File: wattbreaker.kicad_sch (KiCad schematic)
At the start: 33 parts, among them J1 Stomp, J2 Power, U1 TL072

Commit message: v0.1: initial revision
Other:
- moved on the sheet: J1, J2
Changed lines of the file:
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@@
   (junction (at 156.845 55.245) (diameter 0.9144) (color 0 0 0 0))
   (junction (at 160.02 55.245) (diameter 0.9144) (color 0 0 0 0))
-  (no_connect (at 51.435 109.855))
+  (no_connect (at 145.415 87.63))
   (wire (pts (xy 25.4 69.215) (xy 29.845 69.215))
     (stroke (width 0) (type solid) (color 0 0 0 0))
@@
     (stroke (width 0) (type solid) (color 0 0 0 0))
   )
-  (wire (pts (xy 34.29 107.315) (xy 51.435 107.315))
-    (stroke (width 0) (type solid) (color 0 0 0 0))
-  )
-  (wire (pts (xy 34.29 108.585) (xy 34.29 107.315))
-    (stroke (width 0) (type solid) (color 0 0 0 0))
-  )
   (wire (pts (xy 38.1 88.265) (xy 38.1 91.44))
     (stroke (width 0) (type solid) (color 0 0 0 0))
@@
     (stroke (width 0) (type solid) (color 0 0 0 0))
   )
-  (wire (pts (xy 43.815 104.775) (xy 51.435 104.775))
-    (stroke (width 0) (type solid) (color 0 0 0 0))
-  )
-  (wire (pts (xy 43.815 112.395) (xy 51.435 112.395))
-    (stroke (width 0) (type solid) (color 0 0 0 0))
-  )
   (wire (pts (xy 52.07 27.305) (xy 52.07 35.56))
     (stroke (width 0) (type solid) (color 0 0 0 0))
@@
     (stroke (width 0) (type solid) (color 0 0 0 0))
   )
-  (wire (pts (xy 72.39 107.315) (xy 72.39 105.41))
-    (stroke (width 0) (type solid) (color 0 0 0 0))
-  )
-  (wire (pts (xy 72.39 109.855) (xy 74.295 109.855))
-    (stroke (width 0) (type solid) (color 0 0 0 0))
-  )
-  (wire (pts (xy 72.39 111.76) (xy 72.39 109.855))
-    (stroke (width 0) (type solid) (color 0 0 0 0))
-  )
-  (wire (pts (xy 74.295 107.315) (xy 72.39 107.315))
-    (stroke (width 0) (type solid) (color 0 0 0 0))
-  )
   (wire (pts (xy 74.93 27.305) (xy 78.105 27.305))
     (stroke (width 0) (type solid) (color 0 0 0 0))
@@
     (stroke (width 0) (type solid) (color 0 0 0 0))
   )
+  (wire (pts (xy 128.27 85.09) (xy 145.415 85.09))
+    (stroke (width 0) (type solid) (color 0 0 0 0))
+  )
+  (wire (pts (xy 128.27 86.36) (xy 128.27 85.09))
+    (stroke (width 0) (type solid) (color 0 0 0 0))
+  )
   (wire (pts (xy 135.89 55.245) (xy 137.795 55.245))
     (stroke (width 0) (type solid) (color 0 0 0 0))
   )
+  (wire (pts (xy 137.795 82.55) (xy 145.415 82.55))
+    (stroke (width 0) (type solid) (color 0 0 0 0))
+  )
+  (wire (pts (xy 137.795 90.17) (xy 145.415 90.17))
+    (stroke (width 0) (type solid) (color 0 0 0 0))
+  )
   (wire (pts (xy 145.415 55.245) (xy 147.32 55.245))
     (stroke (width 0) (type solid) (color 0 0 0 0))
@@
   )
   (wire (pts (xy 160.02 67.945) (xy 160.02 69.85))
+    (stroke (width 0) (type solid) (color 0 0 0 0))
+  )
+  (wire (pts (xy 166.37 85.09) (xy 166.37 83.185))
+    (stroke (width 0) (type solid) (color 0 0 0 0))
+  )
+  (wire (pts (xy 166.37 87.63) (xy 168.275 87.63))
+    (stroke (width 0) (type solid) (color 0 0 0 0))
+  )
+  (wire (pts (xy 166.37 89.535) (xy 166.37 87.63))
+    (stroke (width 0) (type solid) (color 0 0 0 0))
+  )
+  (wire (pts (xy 168.275 85.09) (xy 166.37 85.09))
     (stroke (width 0) (type solid) (color 0 0 0 0))
   )
@@
     (effects (font (size 1.27 1.27)) (justify right))
   )
-  (global_label "IN" (shape input) (at 43.815 104.775 180)    (property "Intersheet References" "${INTERSHEET_REFS}" (id 0) (at 37.9427 104.6956 0)
+  (global_label "IN" (shape input) (at 137.795 82.55 180)    (property "Intersheet References" "${INTERSHEET_REFS}" (id 0) (at 131.9227 82.4706 0)
       (effects (font (size 1.27 1.27)) (justify right) hide)
     )
     (effects (font (size 1.27 1.27)) (justify right))
   )
-  (global_label "OUT" (shape output) (at 43.815 112.395 180)    (property "Intersheet References" "${INTERSHEET_REFS}" (id 0) (at 36.2493 112.3156 0)
+  (global_label "OUT" (shape output) (at 137.795 90.17 180)    (property "Intersheet References" "${INTERSHEET_REFS}" (id 0) (at 130.2293 90.0906 0)
       (effects (font (size 1.27 1.27)) (justify right) hide)
     )
@@
     )
   )
-  (symbol (lib_id "power:+9V") (at 72.39 105.41 0) (unit 1)
-    (in_bom yes) (on_board yes)
-    (property "Reference" "#PWR07" (id 0) (at 72.39 109.22 0)
-      (effects (font (size 1.27 1.27)) hide)
-    )
-    (property "Value" "+9V" (id 1) (at 72.7583 101.0856 0))
-    (property "Footprint" "" (id 2) (at 72.39 105.41 0)
-      (effects (font (size 1.27 1.27)) hide)
-    )
-    (property "Datasheet" "" (id 3) (at 72.39 105.41 0)
-      (effects (font (size 1.27 1.27)) hide)
-    )
-  )
   (symbol (lib_id "power:+9V") (at 86.36 70.485 0) (unit 1)
     (in_bom yes) (on_board yes)
@@
     )
   )
+  (symbol (lib_id "power:+9V") (at 166.37 83.185 0) (unit 1)
+    (in_bom yes) (on_board yes)
+    (property "Reference" "#PWR07" (id 0) (at 166.37 86.995 0)
+      (effects (font (size 1.27 1.27)) hide)
+    )
+    (property "Value" "+9V" (id 1) (at 166.7383 78.8606 0))
+    (property "Footprint" "" (id 2) (at 166.37 83.185 0)
+      (effects (font (size 1.27 1.27)) hide)
+    )
+    (property "Datasheet" "" (id 3) (at 166.37 83.185 0)
+      (effects (font (size 1.27 1.27)) hide)
+    )
+  )
   (symbol (lib_id "power:GND") (at 29.845 82.55 0) (unit 1)
     (in_bom yes) (on_board yes)
@@
     )
   )
-  (symbol (lib_id "power:GND") (at 34.29 108.585 0) (unit 1)
-    (in_bom yes) (on_board yes)
-    (property "Reference" "#PWR02" (id 0) (at 34.29 114.935 0)
-      (effects (font (size 1.27 1.27)) hide)
-    )
-    (property "Value" "GND" (id 1) (at 34.4043 112.9094 0))
-    (property "Footprint" "" (id 2) (at 34.29 108.585 0)
-      (effects (font (size 1.27 1.27)) hide)
-    )
-    (property "Datasheet" "" (id 3) (at 34.29 108.585 0)
-      (effects (font (size 1.27 1.27)) hide)
-    )
-  )
   (symbol (lib_id "power:GND") (at 59.69 75.565 0) (unit 1)
     (in_bom yes) (on_board yes)
@@
     )
   )
-  (symbol (lib_id "power:GND") (at 72.39 111.76 0) (unit 1)
-    (in_bom yes) (on_board yes)
-    (property "Reference" "#PWR08" (id 0) (at 72.39 118.11 0)
-      (effects (font (size 1.27 1.27)) hide)
-    )
-    (property "Value" "GND" (id 1) (at 72.5043 116.0844 0))
-    (property "Footprint" "" (id 2) (at 72.39 111.76 0)
-      (effects (font (size 1.27 1.27)) hide)
-    )
-    (property "Datasheet" "" (id 3) (at 72.39 111.76 0)
-      (effects (font (size 1.27 1.27)) hide)
-    )
-  )
   (symbol (lib_id "power:GND") (at 99.06 95.885 0) (unit 1)
     (in_bom yes) (on_board yes)
@@
     )
   )
+  (symbol (lib_id "power:GND") (at 128.27 86.36 0) (unit 1)
+    (in_bom yes) (on_board yes)
+    (property "Reference" "#PWR02" (id 0) (at 128.27 92.71 0)
+      (effects (font (size 1.27 1.27)) hide)
+    )
+    (property "Value" "GND" (id 1) (at 128.3843 90.6844 0))
+    (property "Footprint" "" (id 2) (at 128.27 86.36 0)
+      (effects (font (size 1.27 1.27)) hide)
+    )
+    (property "Datasheet" "" (id 3) (at 128.27 86.36 0)
+      (effects (font (size 1.27 1.27)) hide)
+    )
+  )
   (symbol (lib_id "power:GND") (at 160.02 69.85 0) (unit 1)
     (in_bom yes) (on_board yes)
@@
     )
     (property "Datasheet" "" (id 3) (at 160.02 69.85 0)
+      (effects (font (size 1.27 1.27)) hide)
+    )
+  )
+  (symbol (lib_id "power:GND") (at 166.37 89.535 0) (unit 1)
+    (in_bom yes) (on_board yes)
+    (property "Reference" "#PWR08" (id 0) (at 166.37 95.885 0)
+      (effects (font (size 1.27 1.27)) hide)
+    )
+    (property "Value" "GND" (id 1) (at 166.4843 93.8594 0))
+    (property "Footprint" "" (id 2) (at 166.37 89.535 0)
+      (effects (font (size 1.27 1.27)) hide)
+    )
+    (property "Datasheet" "" (id 3) (at 166.37 89.535 0)
       (effects (font (size 1.27 1.27)) hide)
     )
@@
     )
   )
-  (symbol (lib_id "Connector:Conn_01x02_Female") (at 79.375 107.315 0) (unit 1)
-    (in_bom yes) (on_board yes)
-    (property "Reference" "J2" (id 0) (at 80.0863 107.8928 0)
-      (effects (font (size 1.27 1.27)) (justify left))
-    )
-    (property "Value" "Power" (id 1) (at 80.086 110.192 0)
-      (effects (font (size 1.27 1.27)) (justify left))
-    )
-    (property "Footprint" "rockola_kicad_footprints:Power_Header_2pin" (id 2) (at 79.375 107.315 0)
-      (effects (font (size 1.27 1.27)) hide)
-    )
-    (property "Datasheet" "~" (id 3) (at 79.375 107.315 0)
+  (symbol (lib_id "Connector:Conn_01x02_Female") (at 173.355 85.09 0) (unit 1)
+    (in_bom yes) (on_board yes)
+    (property "Reference" "J2" (id 0) (at 174.0663 85.6678 0)
+      (effects (font (size 1.27 1.27)) (justify left))
+    )
+    (property "Value" "Power" (id 1) (at 174.066 87.967 0)
+      (effects (font (size 1.27 1.27)) (justify left))
+    )
+    (property "Footprint" "rockola_kicad_footprints:Power_Header_2pin" (id 2) (at 173.355 85.09 0)
+      (effects (font (size 1.27 1.27)) hide)
+    )
+    (property "Datasheet" "~" (id 3) (at 173.355 85.09 0)
       (effects (font (size 1.27 1.27)) hide)
     )
@@
     )
   )
-  (symbol (lib_id "Connector:Conn_01x04_Female") (at 56.515 107.315 0) (unit 1)
-    (in_bom yes) (on_board yes)
-    (property "Reference" "J1" (id 0) (at 57.2263 107.8928 0)
-      (effects (font (size 1.27 1.27)) (justify left))
-    )
-    (property "Value" "Stomp" (id 1) (at 57.226 110.191 0)
-      (effects (font (size 1.27 1.27)) (justify left))
-    )
-    (property "Footprint" "rockola_kicad_footprints:Stomp_4pin" (id 2) (at 56.515 107.315 0)
-      (effects (font (size 1.27 1.27)) hide)
-    )
-    (property "Datasheet" "~" (id 3) (at 56.515 107.315 0)
-      (effects (font (size 1.27 1.27)) hide)
-    )
+  (symbol (lib_id "Connector:Conn_01x04_Female") (at 150.495 85.09 0) (unit 1)
+    (in_bom yes) (on_board yes)
+    (property "Reference" "J1" (id 0) (at 151.2063 85.6678 0)
+      (effects (font (size 1.27 1.27)) (justify left))
+    )
+    (property "Value" "Stomp" (id 1) (at 151.206 87.966 0)
+      (effects (font (size 1.27 1.27)) (justify left))
+    )
+    (property "Footprint" "rockola_kicad_footprints:Stomp_4pin" (id 2) (at 150.495 85.09 0)
+      (effects (font (size 1.27 1.27)) hide)
+    )
+    (property "Datasheet" "~" (id 3) (at 150.495 85.09 0)
+      (effects (font (size 1.27 1.27)) hide)
+    )

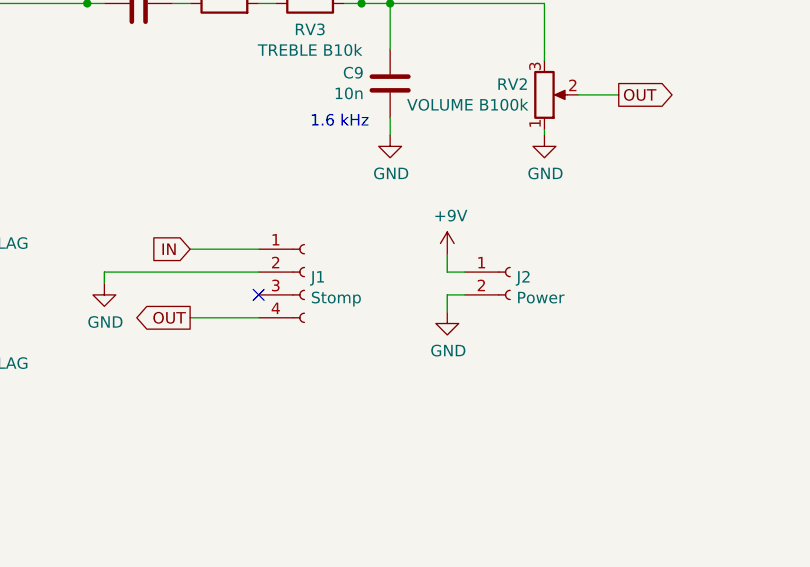
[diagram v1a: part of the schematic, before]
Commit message: updated to KiCad 6.0
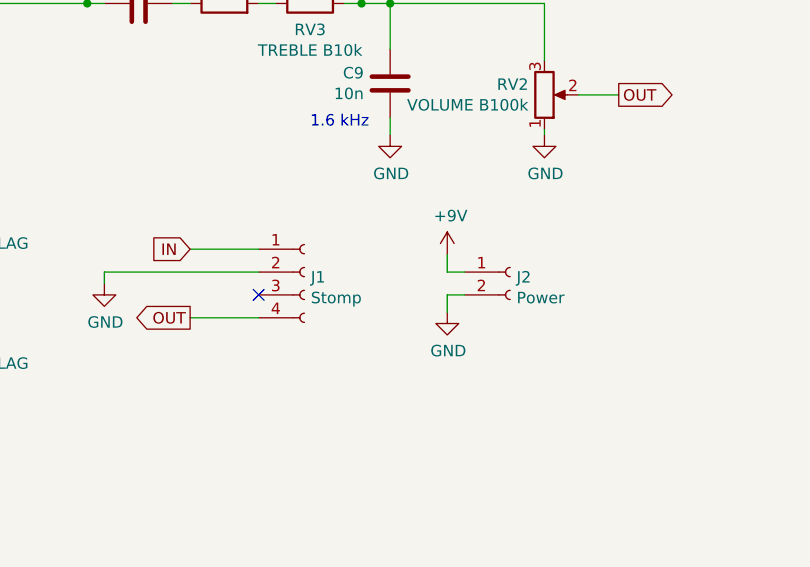
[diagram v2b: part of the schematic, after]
